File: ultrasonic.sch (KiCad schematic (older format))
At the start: 14 parts

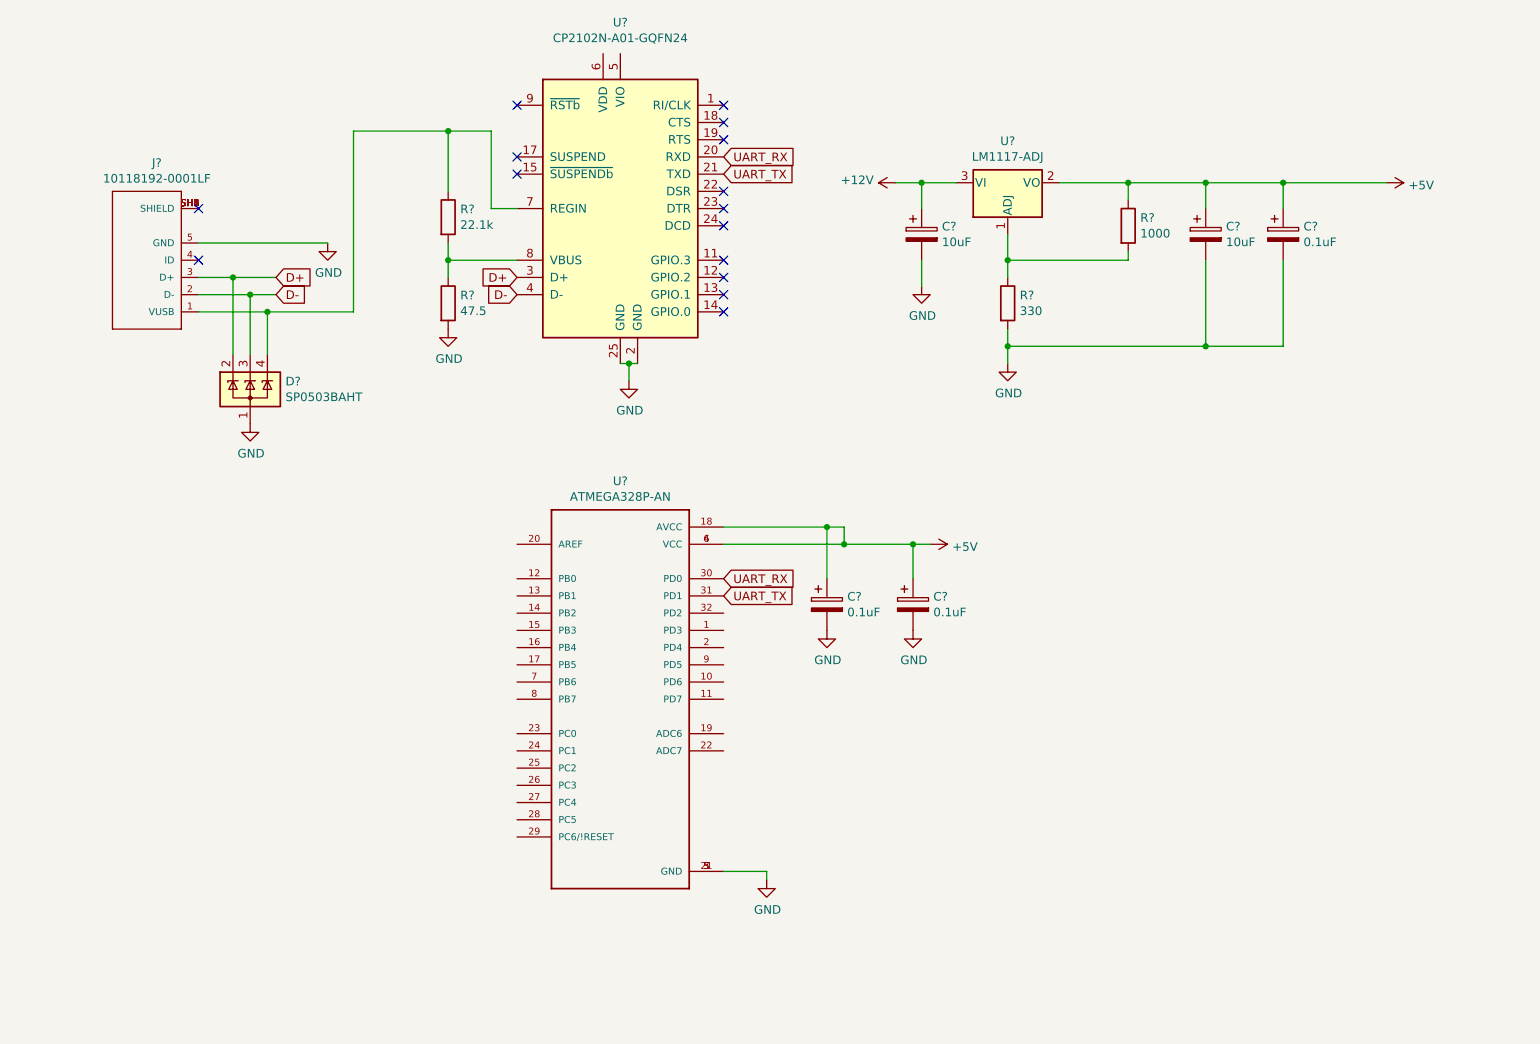
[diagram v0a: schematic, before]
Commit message: Added connectors for ultrasonic
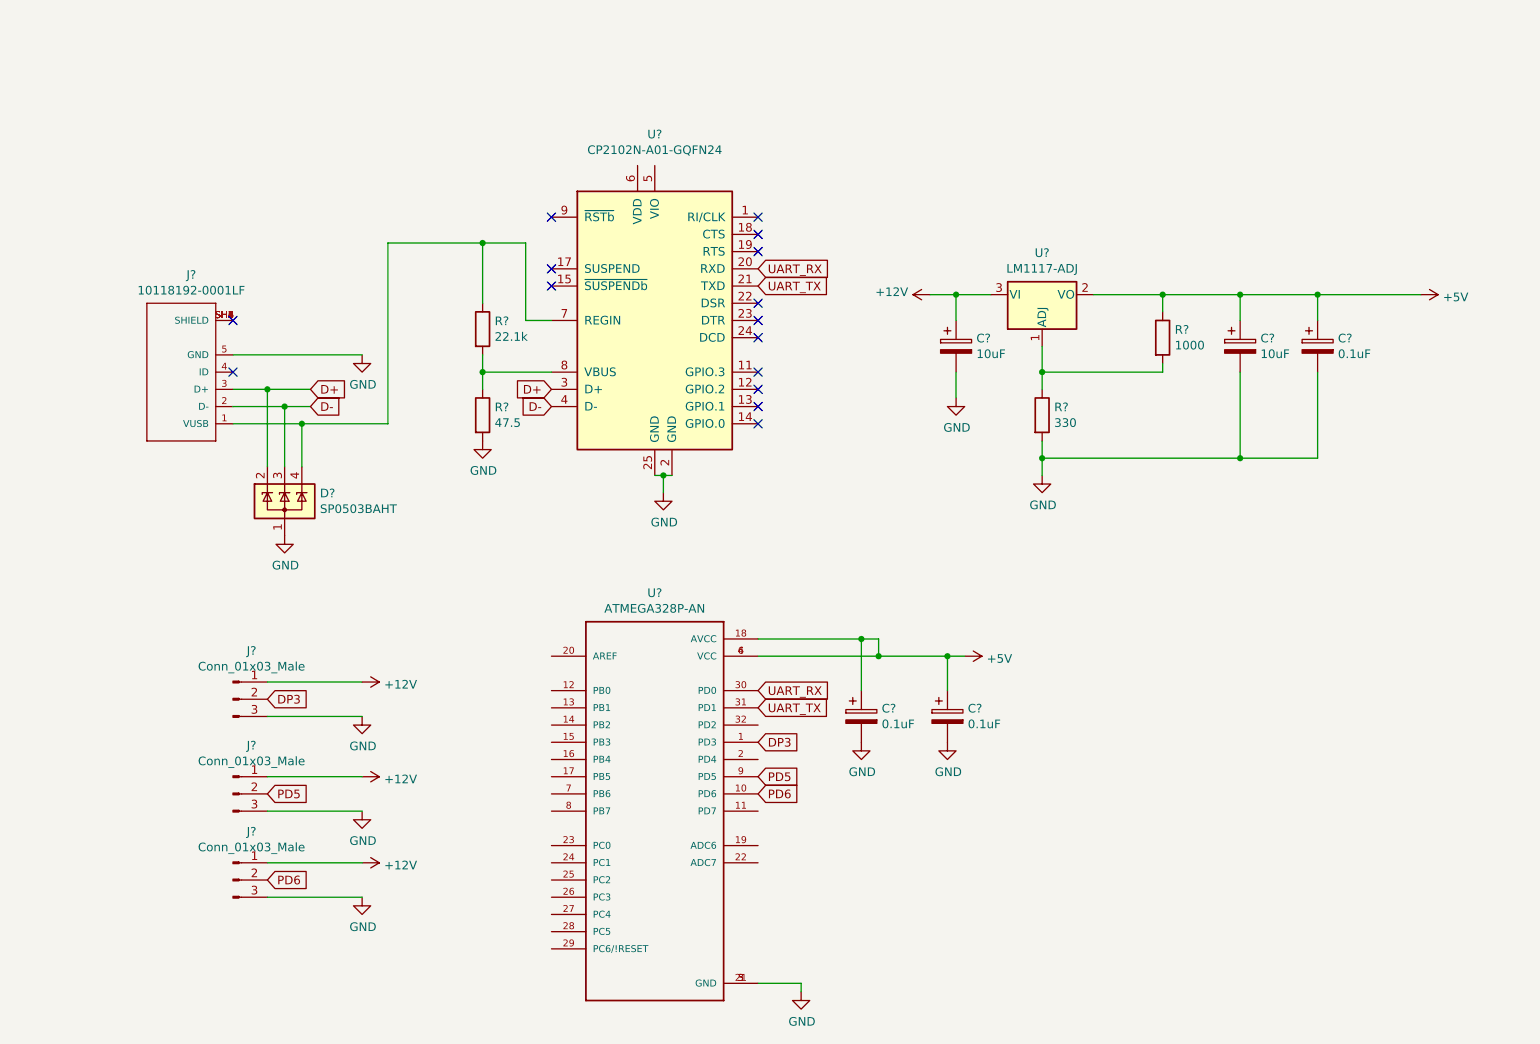
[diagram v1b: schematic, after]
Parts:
- added J? (x3): Conn_01x03_Male, Connector_Molex:Molex_Nano-Fit_105309-xx03_1x03_P2.50mm_Vertical, symbol Connector:Conn_01x03_Male
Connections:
- net +12V: now also J?.1 (Pin_1), J?.1 (Pin_1), J?.1 (Pin_1)
- net GND: now also J?.3 (Pin_3), J?.3 (Pin_3), J?.3 (Pin_3)
- net DP3: now reaches U?.1 (PD3)
- net DP3: now also J?.2 (Pin_2)
- net PD6: now reaches U?.10 (PD6)
- net PD6: now also J?.2 (Pin_2)
- net PD5: now reaches U?.9 (PD5)
- net PD5: now also J?.2 (Pin_2)
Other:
- moved on the sheet: C?, D?, J?, R?, U?

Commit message: Revision 1
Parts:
- added J?: Conn_01x02_Male, Connector_Molex:Molex_Nano-Fit_105309-xx02_1x02_P2.50mm_Vertical, symbol Connector:Conn_01x02_Male
- C1, C2, C3, C4, C5: renamed from C?; footprint (none) -> Capacitor_SMD:C_0805_2012Metric_Pad1.15x1.40mm_HandSolder
- R1, R2, R3, R4: renamed from R?; footprint (none) -> Resistor_SMD:R_0805_2012Metric_Pad1.15x1.40mm_HandSolder
- U3: renamed from U?; footprint (none) -> Package_TO_SOT_SMD:SOT-223-3_TabPin2
- gave numbers to parts that had none: 7
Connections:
- net +12V: now also J?.1 (Pin_1)
- net +5V: now also U1.5 (VIO), U1.6 (VDD)
- net GND: now also J?.2 (Pin_2)
- no-connect marks 15 -> 16
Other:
- moved on the sheet: C1, C2, C3, C4, C5, D1, J1, J2, J3, J4, R1, R2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

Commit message: Final Rev 1
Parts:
- J2, J3, J4: footprint Connector_Molex:Molex_Nano-Fit_105309-xx03_1x03_P2.50mm_Vertical -> Connector_Molex:Molex_SL_171971-0003_1x03_P2.54mm_Vertical
- J5: renamed from J?; footprint Connector_Molex:Molex_Nano-Fit_105309-xx02_1x02_P2.50mm_Vertical -> Connector_Molex:Molex_SL_171971-0002_1x02_P2.54mm_Vertical
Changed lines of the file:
@@
 F 0 "J2" H 3408 4681 50  0000 C CNN
 F 1 "Conn_01x03_Male" H 3408 4590 50  0000 C CNN
-F 2 "Connector_Molex:Molex_Nano-Fit_105309-xx03_1x03_P2.50mm_Vertical" H 3300 4400 50  0001 C CNN
+F 2 "Connector_Molex:Molex_SL_171971-0003_1x03_P2.54mm_Vertical" H 3300 4400 50  0001 C CNN
 F 3 "~" H 3300 4400 50  0001 C CNN
 	1    3300 4400
@@
 F 0 "J3" H 3408 5231 50  0000 C CNN
 F 1 "Conn_01x03_Male" H 3408 5140 50  0000 C CNN
-F 2 "Connector_Molex:Molex_Nano-Fit_105309-xx03_1x03_P2.50mm_Vertical" H 3300 4950 50  0001 C CNN
+F 2 "Connector_Molex:Molex_SL_171971-0003_1x03_P2.54mm_Vertical" H 3300 4950 50  0001 C CNN
 F 3 "~" H 3300 4950 50  0001 C CNN
 	1    3300 4950
@@
 F 0 "J4" H 3408 5781 50  0000 C CNN
 F 1 "Conn_01x03_Male" H 3408 5690 50  0000 C CNN
-F 2 "Connector_Molex:Molex_Nano-Fit_105309-xx03_1x03_P2.50mm_Vertical" H 3300 5500 50  0001 C CNN
+F 2 "Connector_Molex:Molex_SL_171971-0003_1x03_P2.54mm_Vertical" H 3300 5500 50  0001 C CNN
 F 3 "~" H 3300 5500 50  0001 C CNN
 	1    3300 5500
@@
 NoConn ~ 5150 4150
 $Comp
-L Connector:Conn_01x02_Male J?
+L Connector:Conn_01x02_Male J5
 U 1 1 5E44608D
 P 2000 4800
-F 0 "J?" H 2108 4981 50  0000 C CNN
+F 0 "J5" H 2108 4981 50  0000 C CNN
 F 1 "Conn_01x02_Male" H 2108 4890 50  0000 C CNN
-F 2 "Connector_Molex:Molex_Nano-Fit_105309-xx02_1x02_P2.50mm_Vertical" H 2000 4800 50  0001 C CNN
+F 2 "Connector_Molex:Molex_SL_171971-0002_1x02_P2.54mm_Vertical" H 2000 4800 50  0001 C CNN
 F 3 "~" H 2000 4800 50  0001 C CNN
 	1    2000 4800
@@
 $EndComp
 $Comp
-L power:+12V #PWR?
+L power:+12V #PWR0120
 U 1 1 5E45295A
 P 2400 4800
-F 0 "#PWR?" H 2400 4650 50  0001 C CNN
+F 0 "#PWR0120" H 2400 4650 50  0001 C CNN
 F 1 "+12V" V 2415 4928 50  0000 L CNN
 F 2 "" H 2400 4800 50  0001 C CNN
@@
 $EndComp
 $Comp
-L power:GND #PWR?
+L power:GND #PWR0121
 U 1 1 5E45301C
 P 2400 4900
-F 0 "#PWR?" H 2400 4650 50  0001 C CNN
+F 0 "#PWR0121" H 2400 4650 50  0001 C CNN
 F 1 "GND" H 2405 4727 50  0000 C CNN
 F 2 "" H 2400 4900 50  0001 C CNN
